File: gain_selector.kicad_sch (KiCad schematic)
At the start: 7 parts, among them U9 74HC4051

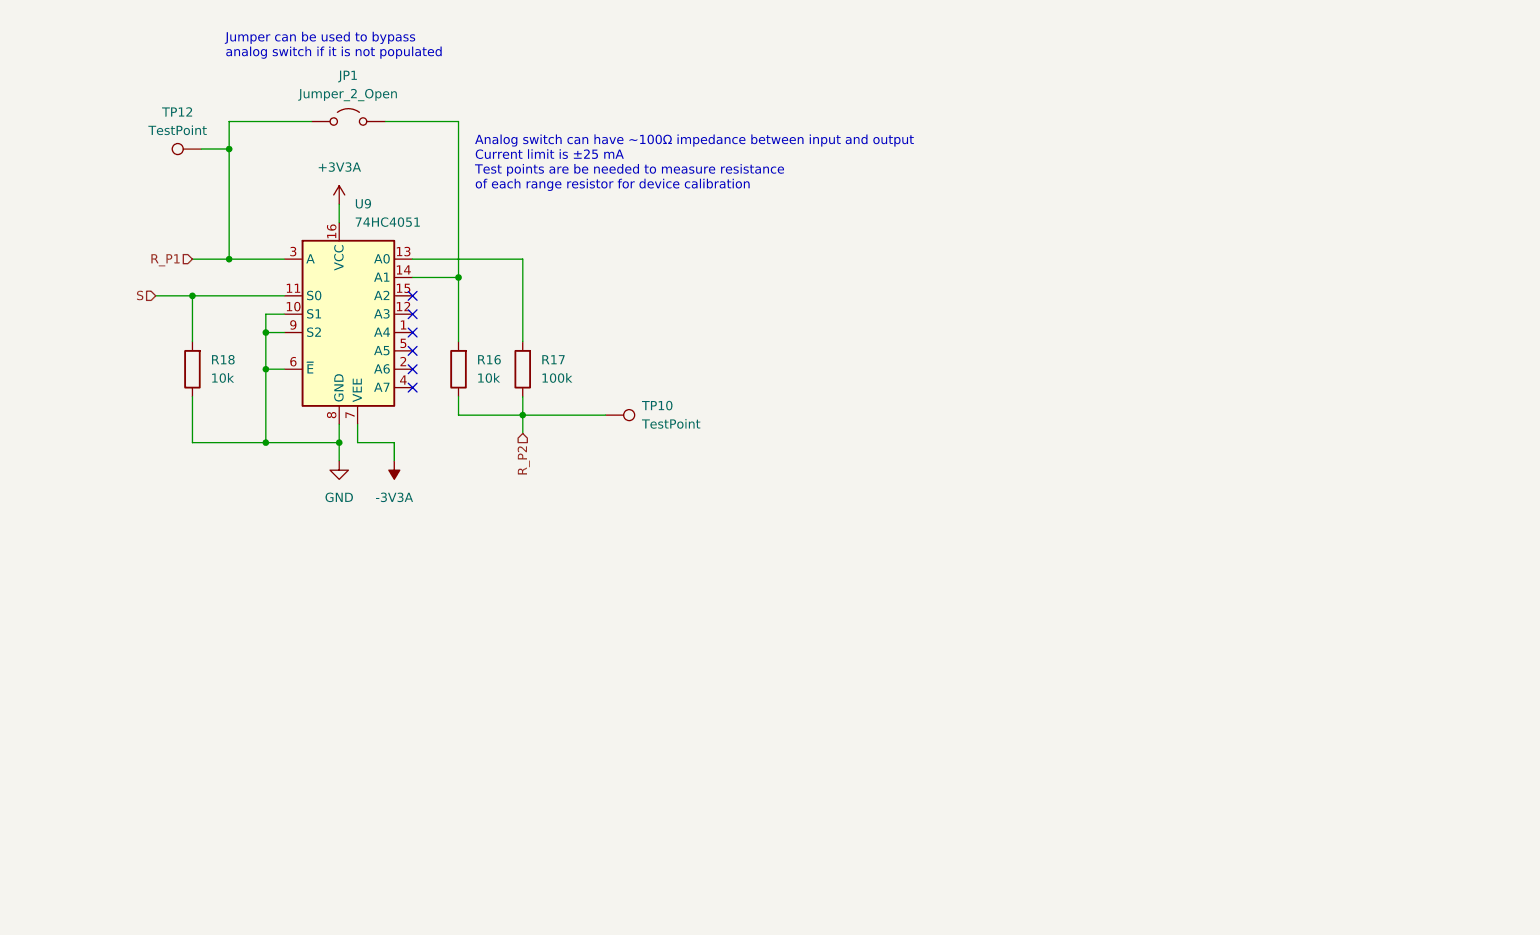
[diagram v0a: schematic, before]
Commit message: Did some routing
Commiting before changing display from i2c to spi
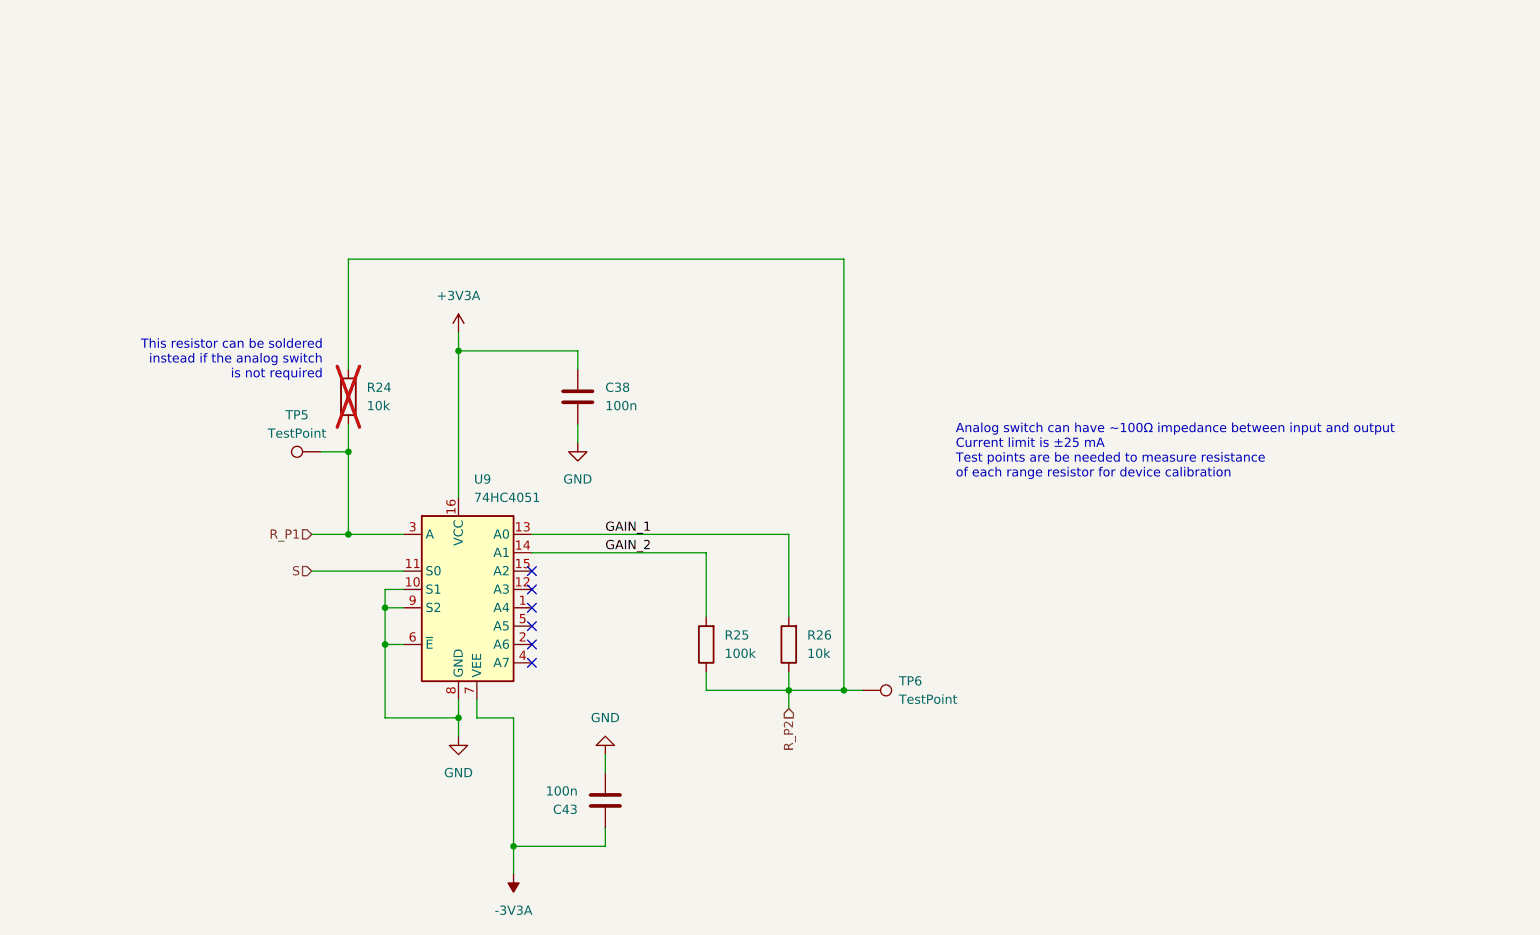
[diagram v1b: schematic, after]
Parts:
- removed JP1: Jumper_2_Open, Jumper:SolderJumper-2_P1.3mm_Open_TrianglePad1.0x1.5mm, symbol Jumper:Jumper_2_Open
- removed R16, R18: 10k, Resistor_SMD:R_0603_1608Metric, symbol Device:R
- removed R17: 100k, Resistor_SMD:R_0603_1608Metric, symbol Device:R
- added C38, C43: 100n, Capacitor_SMD:C_0603_1608Metric, symbol Device:C
- added R24, R26: 10k, Resistor_SMD:R_0603_1608Metric, symbol Device:R
- added R25: 100k, Resistor_SMD:R_0603_1608Metric, symbol Device:R
- renumbered TP12 to TP5, TP10 to TP6
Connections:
- net +3V3A: now also C38.2
- net -3V3A: now also C43.2
- net GND: now also C38.1, C43.1
- net R_P1: now also R24.1
- net R_P2: now also R24.2, R25.1, R26.1
- net GAIN_2: now reaches U9.14 (A1)
- net GAIN_2: now also R25.2
- net GAIN_1: now reaches U9.13 (A0)
- net GAIN_1: now also R26.2
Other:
- note added: "This resistor can be soldered instead if the analog switch is not required"
- note removed: "Jumper can be used to bypass analog switch if it is not populated"
- moved on the sheet: TP5, TP6, U9

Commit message: Done
Schematics and PCB are "done".
Meaning I've just finished but need to review
the design before it's ready to order.
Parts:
- renumbered C43 to C39, R24 to R18, R25 to R19, R26 to R20, TP5 to TP7, TP6 to TP8
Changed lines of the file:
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@@
 		(dnp no)
 		(fields_autoplaced yes)
-		(property "Reference" "#PWR093"
+		(property "Reference" "#PWR081"
 			(at 119.38 137.16 0)
 			(hide yes)
@@
 			(project "lcr"
 				(path "/226ea51e-4da2-4daa-967e-dce167947430/c9f416db-c7a0-48f3-8fda-35fdd9af5fe5/2911f1c4-2f69-429a-9438-24c6ac9b9c30"
-					(reference "#PWR093")
+					(reference "#PWR081")
 					(unit 1)
 				)
@@
 		(dnp no)
 		(fields_autoplaced yes)
-		(property "Reference" "#PWR079"
+		(property "Reference" "#PWR077"
 			(at 111.76 69.85 0)
 			(hide yes)
@@
 			(project "lcr"
 				(path "/226ea51e-4da2-4daa-967e-dce167947430/c9f416db-c7a0-48f3-8fda-35fdd9af5fe5/2911f1c4-2f69-429a-9438-24c6ac9b9c30"
-					(reference "#PWR079")
+					(reference "#PWR077")
 					(unit 1)
 				)
@@
 		(dnp no)
 		(fields_autoplaced yes)
-		(property "Reference" "C43"
+		(property "Reference" "C39"
 			(at 128.27 132.0801 0)
 			(show_name no)
@@
 			(project "lcr"
 				(path "/226ea51e-4da2-4daa-967e-dce167947430/c9f416db-c7a0-48f3-8fda-35fdd9af5fe5/2911f1c4-2f69-429a-9438-24c6ac9b9c30"
-					(reference "C43")
+					(reference "C39")
 					(unit 1)
 				)
@@
 		(dnp no)
 		(fields_autoplaced yes)
-		(property "Reference" "#PWR080"
+		(property "Reference" "#PWR078"
 			(at 128.27 87.63 0)
 			(hide yes)
@@
 			(project "lcr"
 				(path "/226ea51e-4da2-4daa-967e-dce167947430/c9f416db-c7a0-48f3-8fda-35fdd9af5fe5/2911f1c4-2f69-429a-9438-24c6ac9b9c30"
-					(reference "#PWR080")
+					(reference "#PWR078")
 					(unit 1)
 				)
@@
 		(dnp no)
 		(fields_autoplaced yes)
-		(property "Reference" "R25"
+		(property "Reference" "R19"
 			(at 148.59 107.9499 0)
 			(show_name no)
@@
 			(project "lcr"
 				(path "/226ea51e-4da2-4daa-967e-dce167947430/c9f416db-c7a0-48f3-8fda-35fdd9af5fe5/2911f1c4-2f69-429a-9438-24c6ac9b9c30"
-					(reference "R25")
+					(reference "R19")
 					(unit 1)
 				)
@@
 		(dnp yes)
 		(fields_autoplaced yes)
-		(property "Reference" "R24"
+		(property "Reference" "R18"
 			(at 99.06 73.6599 0)
 			(show_name no)
@@
 			(project "lcr"
 				(path "/226ea51e-4da2-4daa-967e-dce167947430/c9f416db-c7a0-48f3-8fda-35fdd9af5fe5/2911f1c4-2f69-429a-9438-24c6ac9b9c30"
-					(reference "R24")
+					(reference "R18")
 					(unit 1)
 				)
@@
 		(dnp no)
 		(fields_autoplaced yes)
-		(property "Reference" "TP6"
+		(property "Reference" "TP8"
 			(at 172.72 114.2999 90)
 			(show_name no)
@@
 			(project "lcr"
 				(path "/226ea51e-4da2-4daa-967e-dce167947430/c9f416db-c7a0-48f3-8fda-35fdd9af5fe5/2911f1c4-2f69-429a-9438-24c6ac9b9c30"
-					(reference "TP6")
+					(reference "TP8")
 					(unit 1)
 				)
@@
 		(dnp no)
 		(fields_autoplaced yes)
-		(property "Reference" "TP5"
+		(property "Reference" "TP7"
 			(at 89.408 77.47 90)
 			(show_name no)
@@
 			(project "lcr"
 				(path "/226ea51e-4da2-4daa-967e-dce167947430/c9f416db-c7a0-48f3-8fda-35fdd9af5fe5/2911f1c4-2f69-429a-9438-24c6ac9b9c30"
-					(reference "TP5")
+					(reference "TP7")
 					(unit 1)
 				)
@@
 		(dnp no)
 		(fields_autoplaced yes)
-		(property "Reference" "R26"
+		(property "Reference" "R20"
 			(at 160.02 107.9499 0)
 			(show_name no)
@@
 			(project "lcr"
 				(path "/226ea51e-4da2-4daa-967e-dce167947430/c9f416db-c7a0-48f3-8fda-35fdd9af5fe5/2911f1c4-2f69-429a-9438-24c6ac9b9c30"
-					(reference "R26")
+					(reference "R20")
 					(unit 1)
 				)
@@
 		(dnp no)
 		(fields_autoplaced yes)
-		(property "Reference" "#PWR094"
+		(property "Reference" "#PWR080"
 			(at 132.08 118.11 0)
 			(hide yes)
@@
 			(project "lcr"
 				(path "/226ea51e-4da2-4daa-967e-dce167947430/c9f416db-c7a0-48f3-8fda-35fdd9af5fe5/2911f1c4-2f69-429a-9438-24c6ac9b9c30"
-					(reference "#PWR094")
+					(reference "#PWR080")
 					(unit 1)
 				)
@@
 		(dnp no)
 		(fields_autoplaced yes)
-		(property "Reference" "#PWR081"
+		(property "Reference" "#PWR079"
 			(at 111.76 128.27 0)
 			(hide yes)
@@
 			(project "lcr"
 				(path "/226ea51e-4da2-4daa-967e-dce167947430/c9f416db-c7a0-48f3-8fda-35fdd9af5fe5/2911f1c4-2f69-429a-9438-24c6ac9b9c30"
-					(reference "#PWR081")
-					(unit 1)
-				)
+					(reference "#PWR079")
+					(unit 1)
+				)

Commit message: Added polish
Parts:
- renumbered R18 to R20, R19 to R21, R20 to R22, TP8 to TP10, TP7 to TP9
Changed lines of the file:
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@@
 		(dnp no)
 		(fields_autoplaced yes)
-		(property "Reference" "#PWR081"
+		(property "Reference" "#PWR087"
 			(at 119.38 137.16 0)
 			(hide yes)
@@
 			(project "lcr"
 				(path "/226ea51e-4da2-4daa-967e-dce167947430/c9f416db-c7a0-48f3-8fda-35fdd9af5fe5/2911f1c4-2f69-429a-9438-24c6ac9b9c30"
-					(reference "#PWR081")
+					(reference "#PWR087")
 					(unit 1)
 				)
@@
 		(dnp no)
 		(fields_autoplaced yes)
-		(property "Reference" "#PWR077"
+		(property "Reference" "#PWR083"
 			(at 111.76 69.85 0)
 			(hide yes)
@@
 			(project "lcr"
 				(path "/226ea51e-4da2-4daa-967e-dce167947430/c9f416db-c7a0-48f3-8fda-35fdd9af5fe5/2911f1c4-2f69-429a-9438-24c6ac9b9c30"
-					(reference "#PWR077")
+					(reference "#PWR083")
 					(unit 1)
 				)
@@
 		(dnp no)
 		(fields_autoplaced yes)
-		(property "Reference" "#PWR078"
+		(property "Reference" "#PWR084"
 			(at 128.27 87.63 0)
 			(hide yes)
@@
 			(project "lcr"
 				(path "/226ea51e-4da2-4daa-967e-dce167947430/c9f416db-c7a0-48f3-8fda-35fdd9af5fe5/2911f1c4-2f69-429a-9438-24c6ac9b9c30"
-					(reference "#PWR078")
+					(reference "#PWR084")
 					(unit 1)
 				)
@@
 		(dnp no)
 		(fields_autoplaced yes)
-		(property "Reference" "R19"
+		(property "Reference" "R21"
 			(at 148.59 107.9499 0)
 			(show_name no)
@@
 			(project "lcr"
 				(path "/226ea51e-4da2-4daa-967e-dce167947430/c9f416db-c7a0-48f3-8fda-35fdd9af5fe5/2911f1c4-2f69-429a-9438-24c6ac9b9c30"
-					(reference "R19")
+					(reference "R21")
 					(unit 1)
 				)
@@
 		(dnp yes)
 		(fields_autoplaced yes)
-		(property "Reference" "R18"
+		(property "Reference" "R20"
 			(at 99.06 73.6599 0)
 			(show_name no)
@@
 			(project "lcr"
 				(path "/226ea51e-4da2-4daa-967e-dce167947430/c9f416db-c7a0-48f3-8fda-35fdd9af5fe5/2911f1c4-2f69-429a-9438-24c6ac9b9c30"
-					(reference "R18")
+					(reference "R20")
 					(unit 1)
 				)
@@
 		(dnp no)
 		(fields_autoplaced yes)
-		(property "Reference" "TP8"
+		(property "Reference" "TP10"
 			(at 172.72 114.2999 90)
 			(show_name no)
@@
 			(project "lcr"
 				(path "/226ea51e-4da2-4daa-967e-dce167947430/c9f416db-c7a0-48f3-8fda-35fdd9af5fe5/2911f1c4-2f69-429a-9438-24c6ac9b9c30"
-					(reference "TP8")
+					(reference "TP10")
 					(unit 1)
 				)
@@
 		(dnp no)
 		(fields_autoplaced yes)
-		(property "Reference" "TP7"
+		(property "Reference" "TP9"
 			(at 89.408 77.47 90)
 			(show_name no)
@@
 			(project "lcr"
 				(path "/226ea51e-4da2-4daa-967e-dce167947430/c9f416db-c7a0-48f3-8fda-35fdd9af5fe5/2911f1c4-2f69-429a-9438-24c6ac9b9c30"
-					(reference "TP7")
+					(reference "TP9")
 					(unit 1)
 				)
@@
 		(dnp no)
 		(fields_autoplaced yes)
-		(property "Reference" "R20"
+		(property "Reference" "R22"
 			(at 160.02 107.9499 0)
 			(show_name no)
@@
 			(project "lcr"
 				(path "/226ea51e-4da2-4daa-967e-dce167947430/c9f416db-c7a0-48f3-8fda-35fdd9af5fe5/2911f1c4-2f69-429a-9438-24c6ac9b9c30"
-					(reference "R20")
+					(reference "R22")
 					(unit 1)
 				)
@@
 		(dnp no)
 		(fields_autoplaced yes)
-		(property "Reference" "#PWR080"
+		(property "Reference" "#PWR086"
 			(at 132.08 118.11 0)
 			(hide yes)
@@
 			(project "lcr"
 				(path "/226ea51e-4da2-4daa-967e-dce167947430/c9f416db-c7a0-48f3-8fda-35fdd9af5fe5/2911f1c4-2f69-429a-9438-24c6ac9b9c30"
-					(reference "#PWR080")
+					(reference "#PWR086")
 					(unit 1)
 				)
@@
 		(dnp no)
 		(fields_autoplaced yes)
-		(property "Reference" "#PWR079"
+		(property "Reference" "#PWR085"
 			(at 111.76 128.27 0)
 			(hide yes)
@@
 			(project "lcr"
 				(path "/226ea51e-4da2-4daa-967e-dce167947430/c9f416db-c7a0-48f3-8fda-35fdd9af5fe5/2911f1c4-2f69-429a-9438-24c6ac9b9c30"
-					(reference "#PWR079")
-					(unit 1)
-				)
+					(reference "#PWR085")
+					(unit 1)
+				)

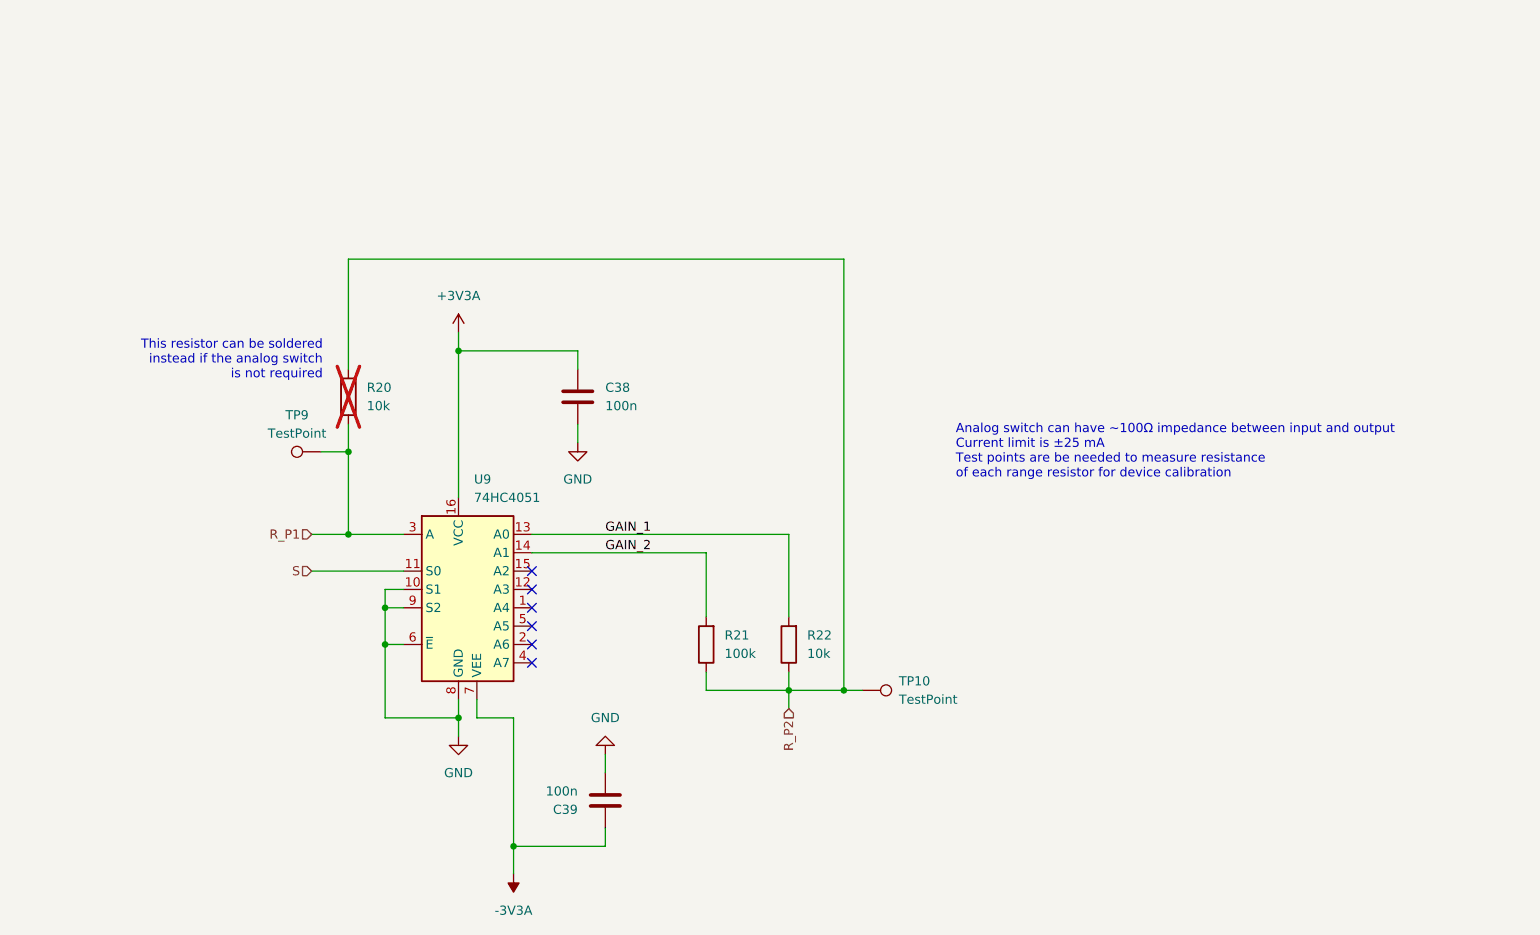
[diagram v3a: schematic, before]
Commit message: Changed range resistor selector design
Changed range resistor selector from an analog mux
to a MOSFET BPS design. This should improve on resistance, linearity,
and temperature stability for the range resistors.
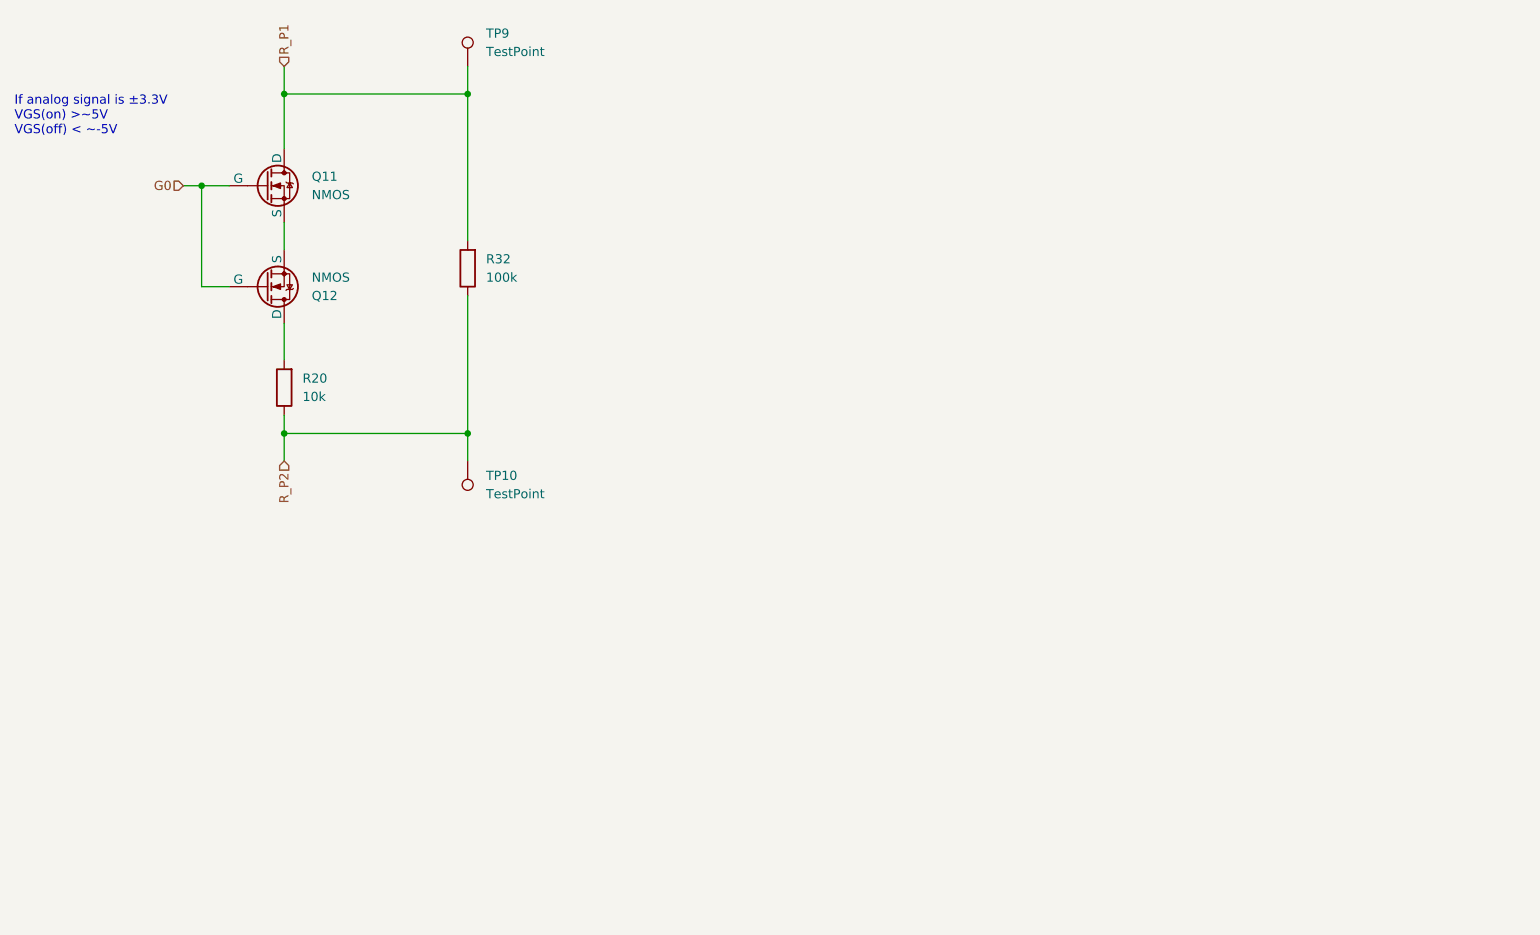
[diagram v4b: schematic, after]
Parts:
- removed C38, C39: 100n, Capacitor_SMD:C_0603_1608Metric, symbol Device:C
- removed R21: 100k, Resistor_SMD:R_0603_1608Metric, symbol Device:R
- removed R22: 10k, Resistor_SMD:R_0603_1608Metric, symbol Device:R
- removed U9: 74HC4051, Package_SO:SOIC-16_3.9x9.9mm_P1.27mm, symbol 74xx:74HC4051
- added Q11, Q12: NMOS, Package_TO_SOT_SMD:SOT-23-3, symbol Simulation_SPICE:NMOS
- added R32: 100k, Resistor_SMD:R_0603_1608Metric, symbol Device:R
- R20: now fitted; now in the parts list
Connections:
- net R_P1: now also Q11.1 (D), R32.2; no longer R20.1
- net R_P2: now also R20.1, R32.1; no longer R20.2
- new net: Q12.1 (D), R20.2
- new net: Q11.3 (S), Q12.3 (S)
- new net G0: Q11.2 (G), Q12.2 (G)
- no-connect marks 6 -> 0
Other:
- note added: "If analog signal is ±3.3V VGS(on) >~5V VGS(off) < ~-5V"
- note removed: "Analog switch can have ~100Ω impedance between input and output Current limit is ±25 mA Test points are be needed to measure resistance of each range resistor for device calibration"
- note removed: "This resistor can be soldered instead if the analog switch is not required"
